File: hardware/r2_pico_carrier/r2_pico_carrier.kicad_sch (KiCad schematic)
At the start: 70 parts, among them J1 5V in, J2 OLED socket, J3 Qwiic, J4 expansion, J5 USB-C 5V in, SW1 display, U1 PCA9517A

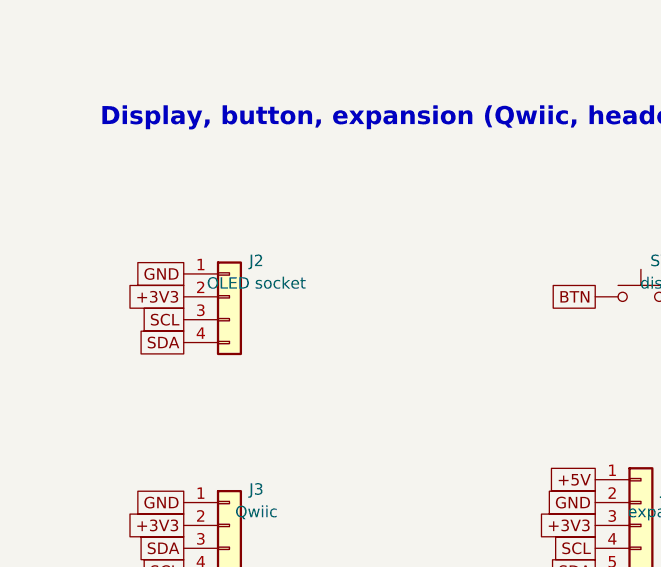
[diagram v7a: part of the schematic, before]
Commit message: Carrier board: J2 is a factory-fitted male header (same part as US1-5); the OLED is soldered on top, flat on the header plastic, instead of plugging into a socket 11 mm up
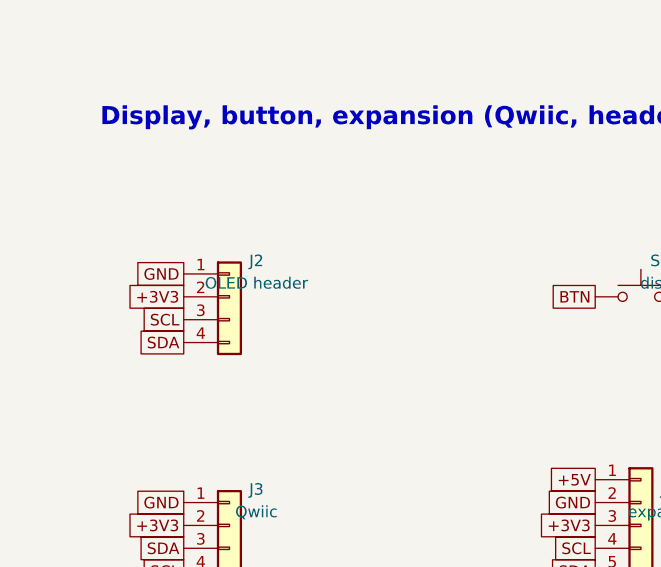
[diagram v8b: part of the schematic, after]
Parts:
- J2: value OLED socket -> OLED header; footprint Connector_PinSocket_2.54mm:PinSocket_1x04_P2.54mm_Vertical -> Connector_PinHeader_2.54mm:PinHeader_1x04_P2.54mm_Vertical; LCSC C2718488 -> C2691448
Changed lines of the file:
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@@
 (global_label "GND" (shape passive) (at 372.11 240.03 180) (fields_autoplaced yes) (effects (font (size 1.27 1.27)) (justify right)))
 (global_label "STAT9_A" (shape passive) (at 379.73 240.03 0) (fields_autoplaced yes) (effects (font (size 1.27 1.27)) (justify left)))
-(symbol (lib_id "Connector_Generic:Conn_01x04") (at 39.37 229.87 0) (unit 1) (exclude_from_sim no) (in_bom yes) (on_board yes) (dnp no) (property "Reference" "J2" (at 42.37 225.87 0) (effects (font (size 1.27 1.27)))) (property "Value" "OLED socket" (at 42.37 228.37 0) (effects (font (size 1.27 1.27)))) (property "Footprint" "Connector_PinSocket_2.54mm:PinSocket_1x04_P2.54mm_Vertical" (at 42.37 230.87 0) (effects (font (size 1.27 1.27)) (hide yes))) (property "Datasheet" "" (at 42.37 233.37 0) (effects (font (size 1.27 1.27)) (hide yes))) (property "LCSC" "C2718488" (at 42.37 235.87 0) (effects (font (size 1.27 1.27)) (hide yes))) (pin "1") (pin "2") (pin "3") (pin "4") (instances (project "r2_pico_carrier" (path "/1e5ddbbd-1ed4-52be-93d8-b73224ab9bea" (reference "J2") (unit 1)))))
+(symbol (lib_id "Connector_Generic:Conn_01x04") (at 39.37 229.87 0) (unit 1) (exclude_from_sim no) (in_bom yes) (on_board yes) (dnp no) (property "Reference" "J2" (at 42.37 225.87 0) (effects (font (size 1.27 1.27)))) (property "Value" "OLED header" (at 42.37 228.37 0) (effects (font (size 1.27 1.27)))) (property "Footprint" "Connector_PinHeader_2.54mm:PinHeader_1x04_P2.54mm_Vertical" (at 42.37 230.87 0) (effects (font (size 1.27 1.27)) (hide yes))) (property "Datasheet" "" (at 42.37 233.37 0) (effects (font (size 1.27 1.27)) (hide yes))) (property "LCSC" "C2691448" (at 42.37 235.87 0) (effects (font (size 1.27 1.27)) (hide yes))) (pin "1") (pin "2") (pin "3") (pin "4") (instances (project "r2_pico_carrier" (path "/1e5ddbbd-1ed4-52be-93d8-b73224ab9bea" (reference "J2") (unit 1)))))
 (global_label "GND" (shape passive) (at 34.29 227.33 180) (fields_autoplaced yes) (effects (font (size 1.27 1.27)) (justify right)))
 (global_label "+3V3" (shape passive) (at 34.29 229.87 180) (fields_autoplaced yes) (effects (font (size 1.27 1.27)) (justify right)))
